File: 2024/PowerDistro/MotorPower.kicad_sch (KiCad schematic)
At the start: 1 part, among them J1 10159560-A00221RLF

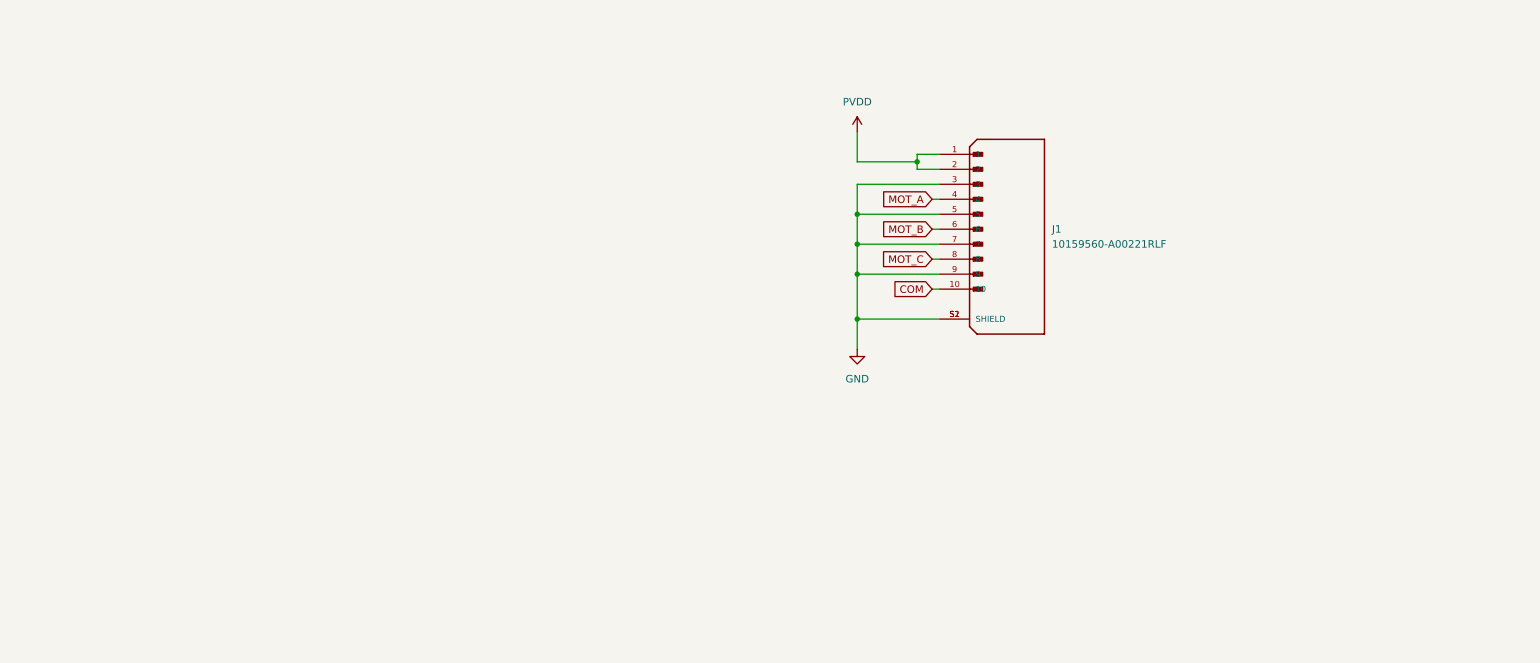
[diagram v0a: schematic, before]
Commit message: Added all other motor power distribution junctions
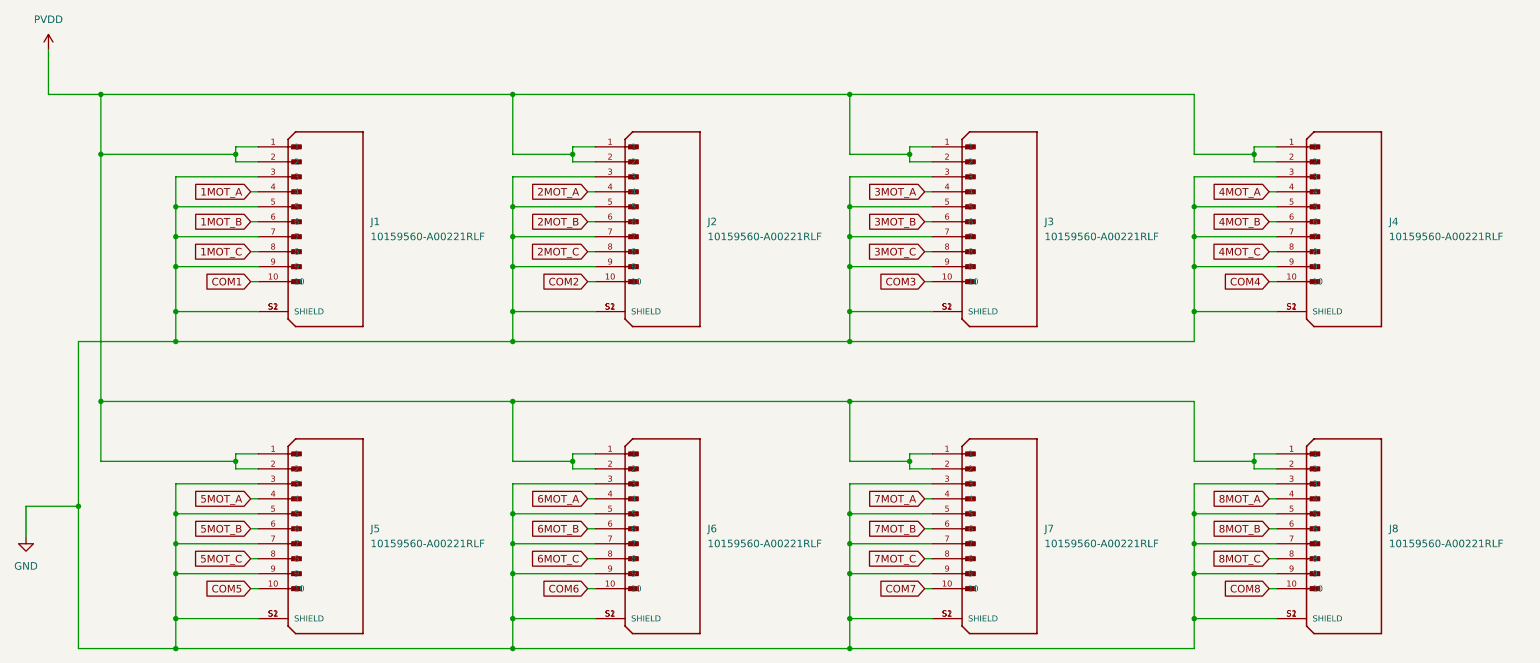
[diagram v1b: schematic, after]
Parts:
- added J1, J2, J4, J5, J6, J7, J8: 10159560-A00221RLF, 10159560-A00221RLF:AMPHENOL_10159560-A00221RLF, symbol PowerDistro:10159560-A00221RLF
- renumbered J1 to J3
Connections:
- net GND: now also J1.3, J1.5, J1.7, J1.9, J1.S1 (SHIELD), J1.S2 (SHIELD), J2.3, J2.5, J2.7, J2.9, J2.S1 (SHIELD), J2.S2 (SHIELD), J4.3, J4.5, J4.7, J4.9, J4.S1 (SHIELD), J4.S2 (SHIELD), J5.3, J5.5, J5.7, J5.9, J5.S1 (SHIELD), J5.S2 (SHIELD), J6.3, J6.5, J6.7, J6.9, J6.S1 (SHIELD), J6.S2 (SHIELD), J7.3, J7.5, J7.7, J7.9, J7.S1 (SHIELD), J7.S2 (SHIELD), J8.3, J8.5, J8.7, J8.9, J8.S1 (SHIELD), J8.S2 (SHIELD)
- net PVDD: now also J1.1, J1.2, J2.1, J2.2, J4.1, J4.2, J5.1, J5.2, J6.1, J6.2, J7.1, J7.2, J8.1, J8.2
- net COM renamed COM3
- net MOT_A renamed 3MOT_A
- net MOT_B renamed 3MOT_B
- net MOT_C renamed 3MOT_C
- new net 1MOT_A: J1.4
- new net 1MOT_B: J1.6
- new net 1MOT_C: J1.8
- new net 2MOT_A: J2.4
- new net 2MOT_B: J2.6
- new net 2MOT_C: J2.8
- new net 4MOT_A: J4.4
- new net 4MOT_B: J4.6
- new net 4MOT_C: J4.8
- new net 5MOT_A: J5.4
- new net 5MOT_B: J5.6
- new net 5MOT_C: J5.8
- new net 6MOT_A: J6.4
- new net 6MOT_B: J6.6
- new net 6MOT_C: J6.8
- new net 7MOT_A: J7.4
- new net 7MOT_B: J7.6
- new net 7MOT_C: J7.8
- new net 8MOT_A: J8.4
- new net 8MOT_B: J8.6
- new net 8MOT_C: J8.8
- new net COM1: J1.10
- new net COM2: J2.10
- new net COM4: J4.10
- new net COM5: J5.10
- new net COM6: J6.10
- new net COM7: J7.10
- new net COM8: J8.10
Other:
- moved on the sheet: J3
